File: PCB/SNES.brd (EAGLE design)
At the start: 58.5 x 61 mm, 22 parts, among them U1A SN74AHCT125N, U2A SN74AHCT125N, U3A SN74AHCT125N

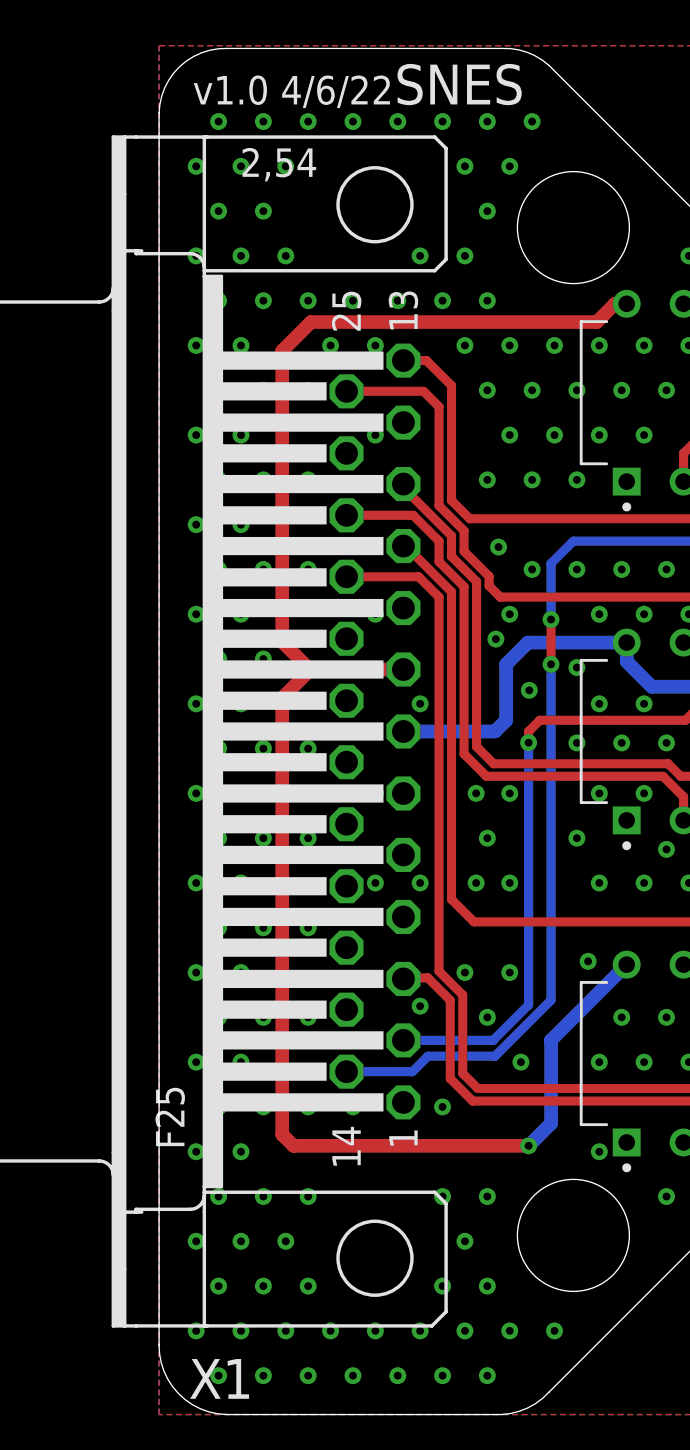
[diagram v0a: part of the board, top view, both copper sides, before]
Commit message: Added exposed GND plane at DB25 anchors
All PCBs have been update to have exposed GND plane pads for the DB25 anchor points.

This resolves Issue 54
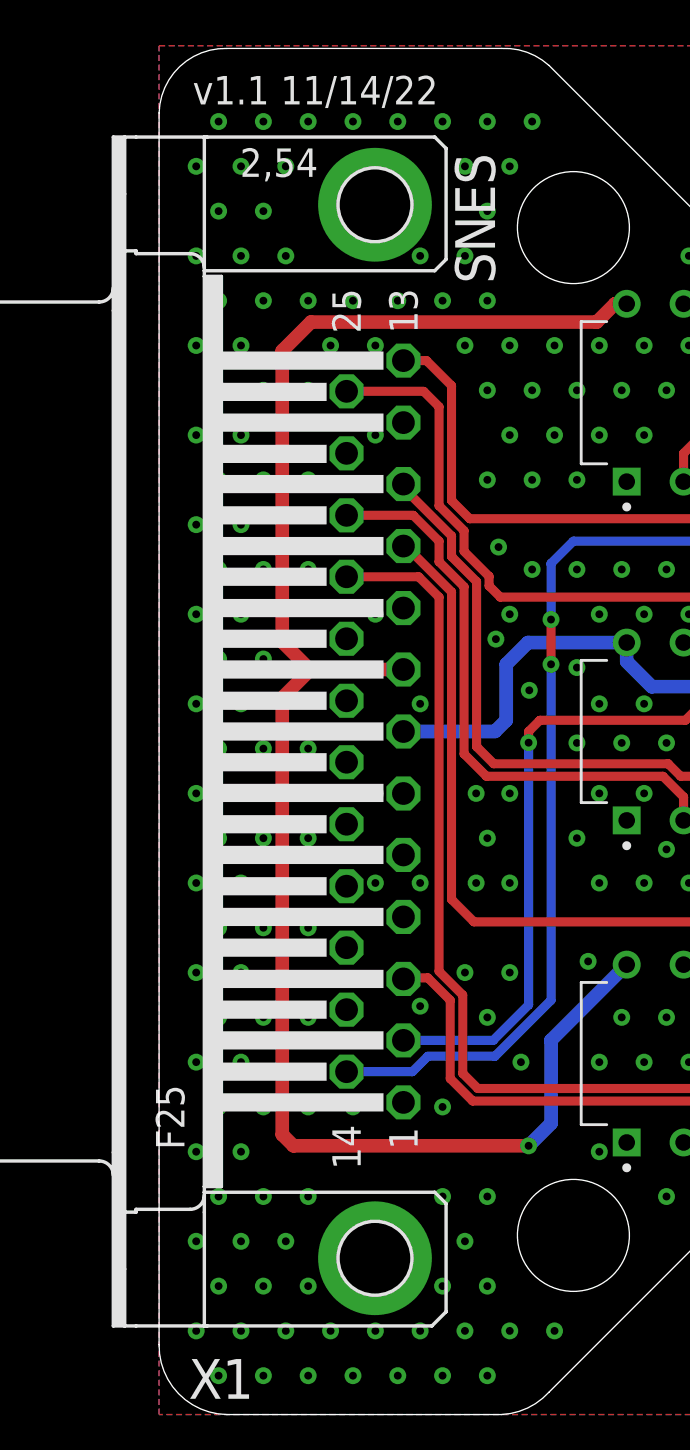
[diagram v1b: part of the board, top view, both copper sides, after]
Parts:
- X1: device SparkFun-Retired:F25H -> SparkFun-Retired:F25HP
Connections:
- net GND: now also X1.GND1, X1.GND2
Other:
- board text added: "v1.1 11/14/22"
- board text removed: "v1.0 4/6/22"
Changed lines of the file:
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@@
 <hole x="18.5" y="53" drill="5"/>
 <hole x="18.5" y="8" drill="5"/>
-<text x="1.5" y="58.5" size="1.27" layer="21">v1.0 4/6/22</text>
-<text x="10.5" y="58.5" size="1.778" layer="21">SNES</text>
+<text x="1.5" y="58.5" size="1.27" layer="21">v1.1 11/14/22</text>
+<text x="15" y="50.5" size="1.778" layer="21" rot="R90">SNES</text>
 <wire x1="58.5" y1="46.377359375" x2="58.5" y2="43.5" width="0" layer="20"/>
 <wire x1="58.5" y1="43.5" x2="56.5" y2="41.5" width="0" layer="20" curve="-90"/>
@@
 <attribute name="PURCHASE-URL" value="https://pricing.snapeda.com/search/part/SN74AHCT125N/?ref=eda" x="149.15" y="71.14" size="1.778" layer="27" rot="R90" display="off"/>
 </element>
-<element name="X1" library="SparkFun-Retired" package="F25H" value="" x="9.64" y="30.5" smashed="yes" rot="R90">
+<element name="X1" library="SparkFun-Retired" package="F25HP" value="" x="9.64" y="30.5" smashed="yes" rot="R90">
 <attribute name="NAME" x="4.219" y="2.48" size="1.778" layer="25" ratio="10" rot="R180"/>
 <attribute name="VALUE" x="-4.33" y="22.118" size="1.778" layer="27" ratio="10" rot="R90"/>
@@
 <via x="55.6568" y="43.735840625" extent="1-16" drill="0.35"/>
 <via x="56.6568" y="45.735840625" extent="1-16" drill="0.35"/>
+<contactref element="X1" pad="GND1"/>
+<contactref element="X1" pad="GND2"/>
 </signal>
 <signal name="5VIN">

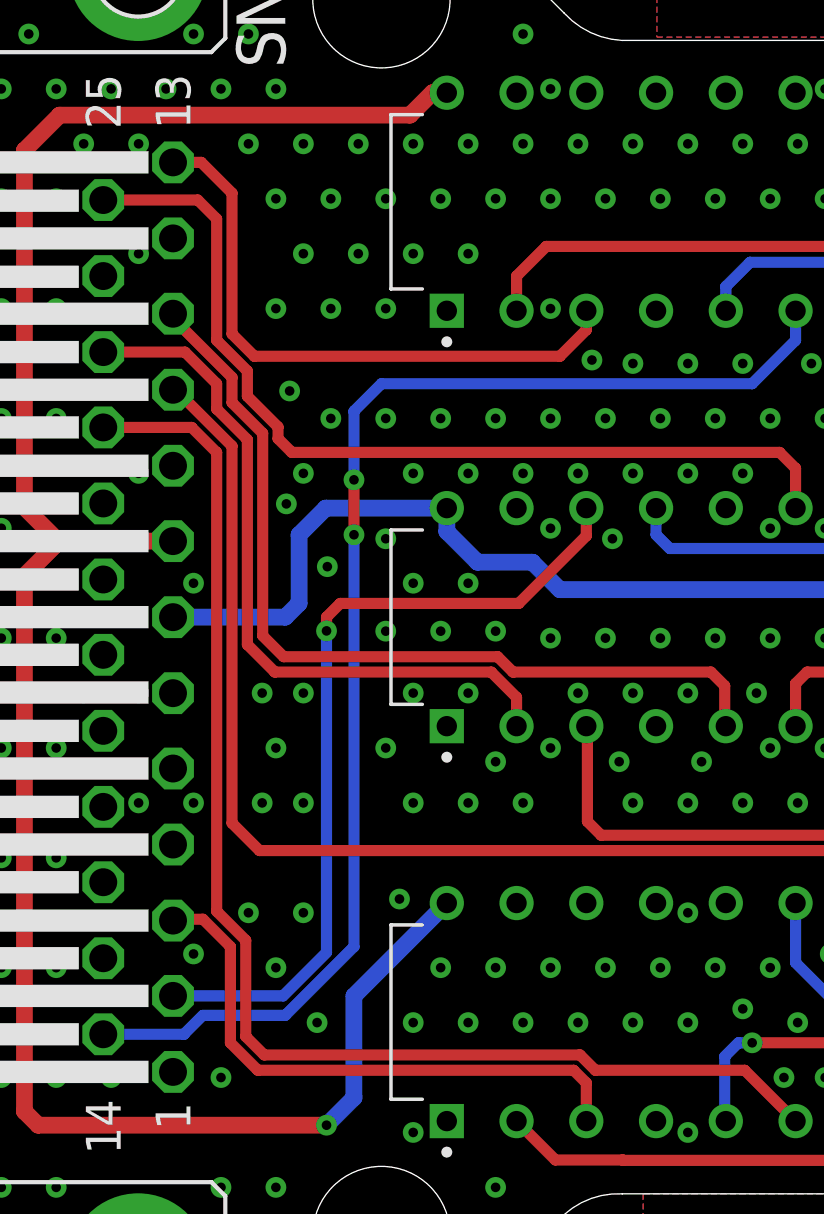
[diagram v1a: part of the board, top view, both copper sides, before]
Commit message: Silkscreen Update, Library Add, Datasheet Add
Updated the silkscreen on all PCBs that used the SN74 components as there was not orientation marker on the silkscreen.

Added Modified SN74 libraries and VB Cable Pinout image
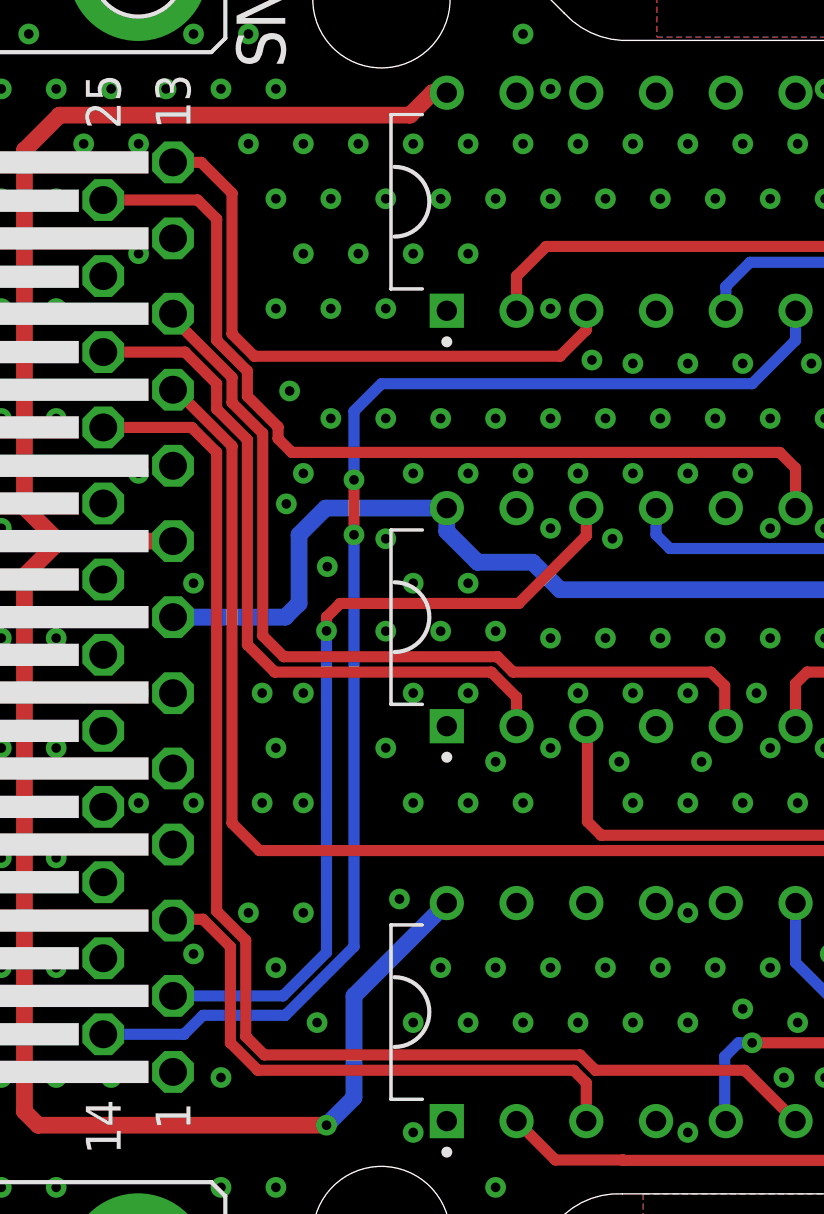
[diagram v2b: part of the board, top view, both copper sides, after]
